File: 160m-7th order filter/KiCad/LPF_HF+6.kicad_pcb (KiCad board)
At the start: 2 copper layers, 250 x 160 mm, 131 parts, among them J1 Conn_01x07, J2 12V INPUT, J3 LFP_IN, J4 Conn_01x07, J5 RF output, U1 AMS1117-5, U2 74AHC595, U3 ULN2003

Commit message: 160m Cheby7
Created and Updated 160m 7th Order Filter Design
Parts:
- added C52: 2005pF, LPF_Footprints:4x1206_2, B.Cu at (117.7, 100.1)
- added L22: T130-10, LPF_Footprints:T106-Inductor, F.Cu at (117.5, 109.9)
- C15: footprint Capacitor_SMD:C_1206_3216Metric -> Capacitor_SMD:C_1206_3216Metric_Pad1.33x1.80mm_HandSolder
- C26: value C_Small -> 2005pF; footprint LPF_Footprints:6x1206 -> LPF_Footprints:4x1206_2
- C31, C37: value 834p -> 1480p
- C32, C38: value C_Small -> 3560pF
- D16, D17, D18, D21, D22, D7, D8, D9: value SD12_SOD323 -> TVS SD12_SOD323
- D19, D20: value Schottky -> 1n4148 Schottky
- L12, L6: value L -> T130-10
- moved C32 38.6 mm to (117.4, 161.8), turned to 180 degrees
- moved C38 24.6 mm to (117.4, 133.8)
- moved L12 22.9 mm to (117.5, 137.2)
- moved L6 16.2 mm to (117.7, 164.5)
- moved C26 9.20 mm to (118.3, 177.4), turned to 45 degrees
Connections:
- REL12 pad 4: Net-(C38-Pad1) -> Net-(C52-Pad1)
- REL12 pad 7: Net-(C38-Pad1) -> Net-(C52-Pad1)
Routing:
- net Net-(C52-Pad1): track 0.00 -> 35.4 mm
- net Net-(C38-Pad1): track 39.7 -> 14.6 mm
- net Net-(C26-Pad1): track 43.6 -> 27.4 mm
- net Net-(C32-Pad1): track 21.3 -> 14.7 mm
- net GND: vias 1017 -> 1020

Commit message: General Save
Minor updates and improvements
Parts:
- C32, C38: footprint LPF_Footprints:6x1206 -> LPF_Footprints:6x1206_3x2
- L1, L13, L7: value L -> Air core; footprint LPF_Footprints:T94-Inductor -> LPF_Footprints:T106-Inductor
- L10, L11, L14, L15, L16, L17, L2, L3, L4, L5, L8, L9: value L -> T106-10; footprint LPF_Footprints:T94-Inductor -> LPF_Footprints:T106-Inductor
- moved C32 0.69 mm to (117.4, 161.1)
- moved L19 0.24 mm to (312.8, 149.4)

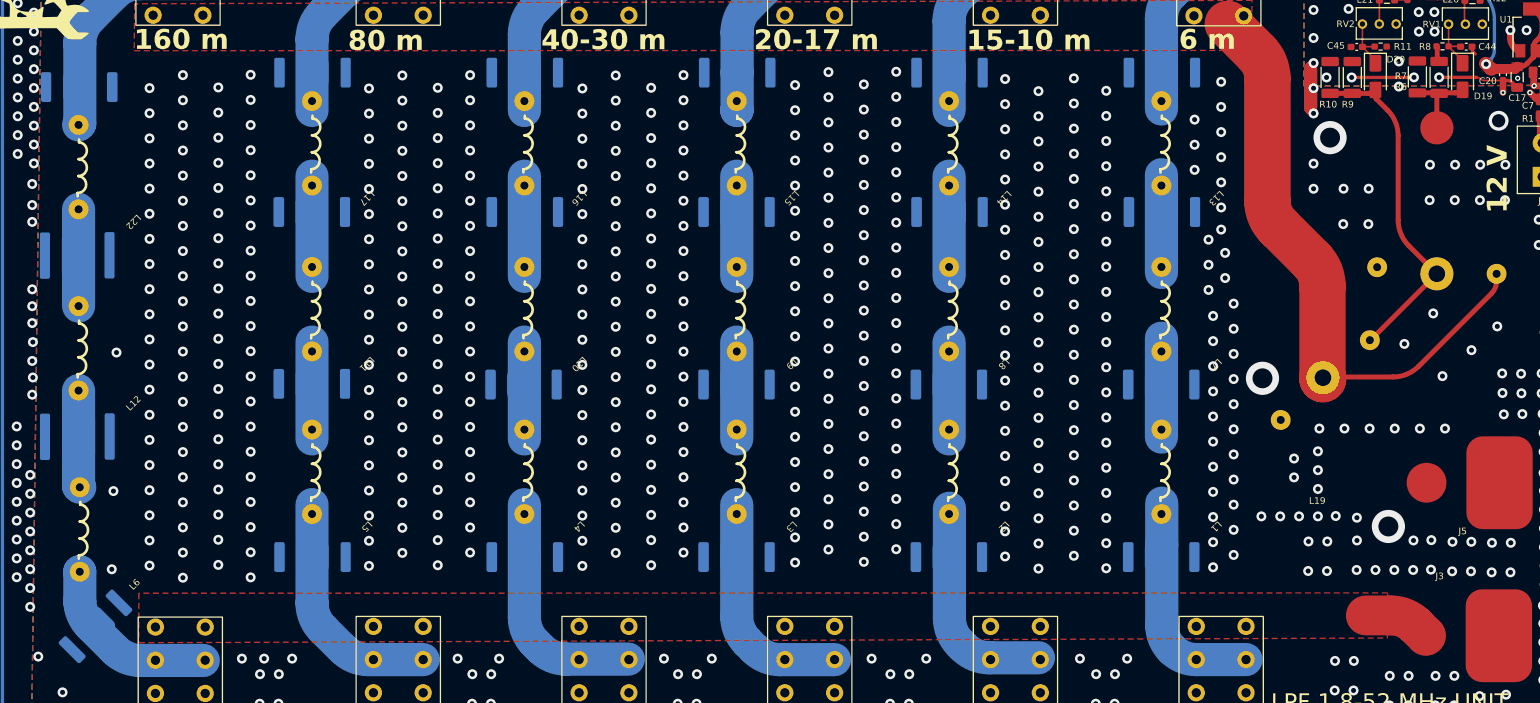
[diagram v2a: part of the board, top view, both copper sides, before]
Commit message: LPF capacitor and toroid selections improved
Added separate sheet for documenting capacitor makeup.
reflected in BOM much more accurately.
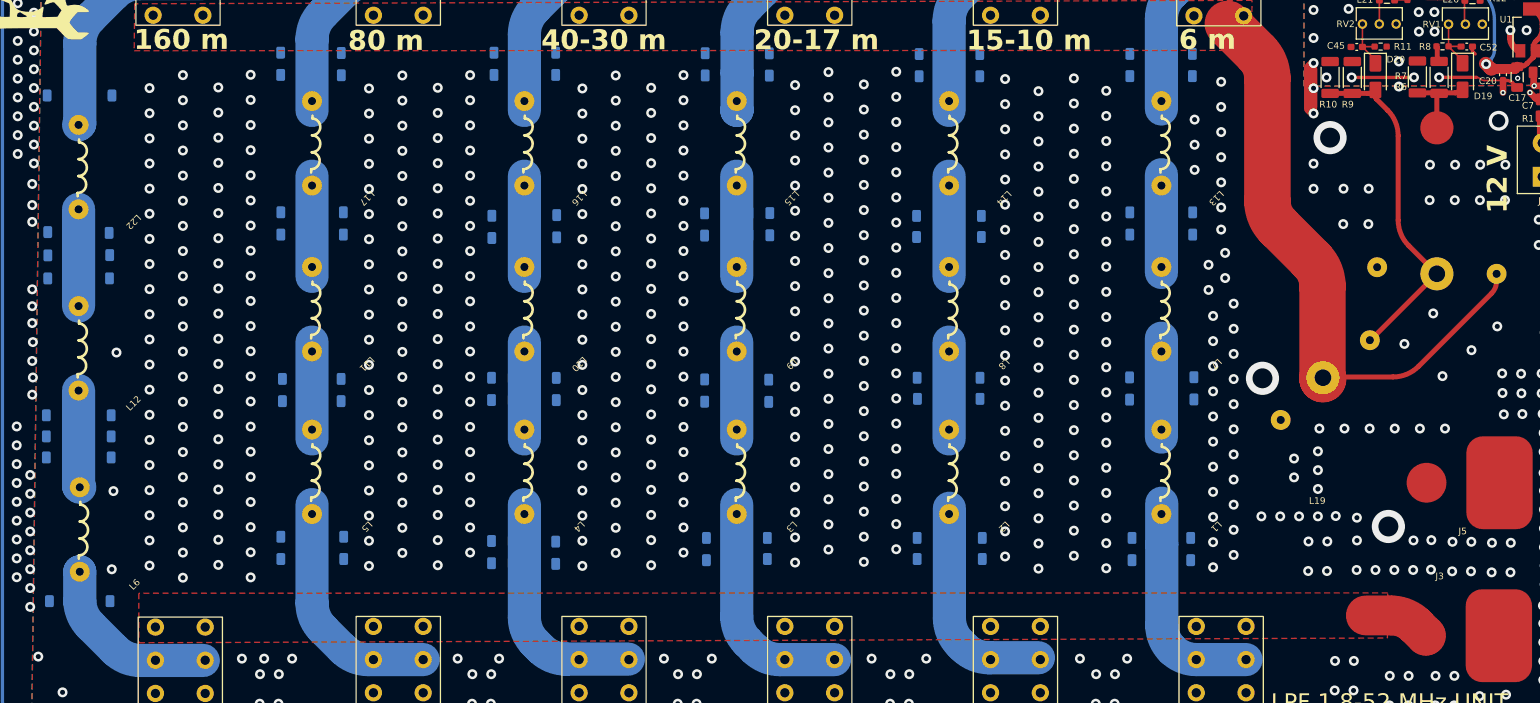
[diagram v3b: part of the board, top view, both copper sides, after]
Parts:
- removed C21, C39: 71p, LPF_Footprints:4x1206_2
- removed C22, C40: 123p, LPF_Footprints:4x1206_2
- removed C23, C41: 203p, LPF_Footprints:4x1206_2
- removed C24, C42: 357p, LPF_Footprints:4x1206_2
- removed C25, C43: 834p, LPF_Footprints:4x1206_2
- removed C26: 2005pF, LPF_Footprints:4x1206_2
- removed C27, C33: 127p, LPF_Footprints:4x1206_2
- removed C28, C34: 218p, LPF_Footprints:4x1206_2
- removed C29, C35: 360p, LPF_Footprints:4x1206_2
- removed C30, C36: 635p, LPF_Footprints:4x1206_2
- removed C31, C37: 1480p, LPF_Footprints:4x1206_2
- removed C32, C38: 3560pF, LPF_Footprints:6x1206_3x2
- removed C44: 100n, Capacitor_SMD:C_0603_1608Metric_Pad1.08x0.95mm_HandSolder
- added C21.1: 33p, Capacitor_SMD:C_1206_3216Metric_Pad1.33x1.80mm_HandSolder, B.Cu at (277.8, 165.7)
- added C21.2: 22p, Capacitor_SMD:C_1206_3216Metric_Pad1.33x1.80mm_HandSolder, B.Cu at (277.8, 169.1)
- added C21.3: 10p, Capacitor_SMD:C_1206_3216Metric_Pad1.33x1.80mm_HandSolder, B.Cu at (283.5, 169.1)
- added C21.4: 10p, Capacitor_SMD:C_1206_3216Metric_Pad1.33x1.80mm_HandSolder, B.Cu at (283.5, 165.7)
- added C22.1: 47p, Capacitor_SMD:C_1206_3216Metric_Pad1.33x1.80mm_HandSolder, B.Cu at (245.4, 165.7)
- added C22.2: 33p, Capacitor_SMD:C_1206_3216Metric_Pad1.33x1.80mm_HandSolder, B.Cu at (245.4, 168.9)
- added C22.3: 33p, Capacitor_SMD:C_1206_3216Metric_Pad1.33x1.80mm_HandSolder, B.Cu at (252.1, 165.7)
- added C22.4: 10p, Capacitor_SMD:C_1206_3216Metric_Pad1.33x1.80mm_HandSolder, B.Cu at (252.1, 168.9)
- added C23.1: 51p, Capacitor_SMD:C_1206_3216Metric_Pad1.33x1.80mm_HandSolder, B.Cu at (213.7, 165.7)
- added C23.2: 51p, Capacitor_SMD:C_1206_3216Metric_Pad1.33x1.80mm_HandSolder, B.Cu at (213.7, 169.1)
- added C23.3: 51p, Capacitor_SMD:C_1206_3216Metric_Pad1.33x1.80mm_HandSolder, B.Cu at (219.7, 165.7)
- added C23.4: 51p, Capacitor_SMD:C_1206_3216Metric_Pad1.33x1.80mm_HandSolder, B.Cu at (219.7, 168.9)
- added C24.1: 100p, Capacitor_SMD:C_1206_3216Metric_Pad1.33x1.80mm_HandSolder, B.Cu at (181.3, 166.2)
- added C24.2: 100p, Capacitor_SMD:C_1206_3216Metric_Pad1.33x1.80mm_HandSolder, B.Cu at (181.3, 169.5)
- added C24.3: 100p, Capacitor_SMD:C_1206_3216Metric_Pad1.33x1.80mm_HandSolder, B.Cu at (187.8, 169.6)
- added C24.4: 51p, Capacitor_SMD:C_1206_3216Metric_Pad1.33x1.80mm_HandSolder, B.Cu at (187.8, 166.3)
- added C25.1: 220p, Capacitor_SMD:C_1206_3216Metric_Pad1.33x1.80mm_HandSolder, B.Cu at (149.5, 165.6)
- added C25.2: 220p, Capacitor_SMD:C_1206_3216Metric_Pad1.33x1.80mm_HandSolder, B.Cu at (149.5, 168.9)
- added C25.3: 220p, Capacitor_SMD:C_1206_3216Metric_Pad1.33x1.80mm_HandSolder, B.Cu at (155.9, 168.9)
- added C25.4: 180p, Capacitor_SMD:C_1206_3216Metric_Pad1.33x1.80mm_HandSolder, B.Cu at (155.9, 165.6)
- added C26.1: 1000p, Capacitor_SMD:C_1206_3216Metric_Pad1.33x1.80mm_HandSolder, B.Cu at (120.7, 175.3)
- added C26.2: 1000p, Capacitor_SMD:C_1206_3216Metric_Pad1.33x1.80mm_HandSolder, B.Cu at (114.6, 175.3)
- added C27.1: 33p, Capacitor_SMD:C_1206_3216Metric_Pad1.33x1.80mm_HandSolder, B.Cu at (277.4, 141.5)
- added C27.2: 33p, Capacitor_SMD:C_1206_3216Metric_Pad1.33x1.80mm_HandSolder, B.Cu at (277.4, 144.9)
- added C27.3: 33p, Capacitor_SMD:C_1206_3216Metric_Pad1.33x1.80mm_HandSolder, B.Cu at (284.0, 144.9)
- added C27.4: 22p, Capacitor_SMD:C_1206_3216Metric_Pad1.33x1.80mm_HandSolder, B.Cu at (284.0, 141.5)
- added C28.1: 100p, Capacitor_SMD:C_1206_3216Metric_Pad1.33x1.80mm_HandSolder, B.Cu at (251.8, 141.6)
- added C28.2: 47p, Capacitor_SMD:C_1206_3216Metric_Pad1.33x1.80mm_HandSolder, B.Cu at (251.8, 144.8)
- added C28.3: 47p, Capacitor_SMD:C_1206_3216Metric_Pad1.33x1.80mm_HandSolder, B.Cu at (245.5, 144.8)
- added C28.4: 22p, Capacitor_SMD:C_1206_3216Metric_Pad1.33x1.80mm_HandSolder, B.Cu at (245.4, 141.6)
- added C29.1: 220p, Capacitor_SMD:C_1206_3216Metric_Pad1.33x1.80mm_HandSolder, B.Cu at (213.4, 141.9)
- added C29.2: 47p, Capacitor_SMD:C_1206_3216Metric_Pad1.33x1.80mm_HandSolder, B.Cu at (213.4, 145.2)
- added C29.3: 47p, Capacitor_SMD:C_1206_3216Metric_Pad1.33x1.80mm_HandSolder, B.Cu at (219.9, 145.2)
- added C29.4: 47p, Capacitor_SMD:C_1206_3216Metric_Pad1.33x1.80mm_HandSolder, B.Cu at (219.9, 141.9)
- added C30.1: 180p, Capacitor_SMD:C_1206_3216Metric_Pad1.33x1.80mm_HandSolder, B.Cu at (181.3, 141.6)
- added C30.2: 180p, Capacitor_SMD:C_1206_3216Metric_Pad1.33x1.80mm_HandSolder, B.Cu at (181.3, 145.0)
- added C30.3: 180p, Capacitor_SMD:C_1206_3216Metric_Pad1.33x1.80mm_HandSolder, B.Cu at (187.9, 145.0)
- added C30.4: 100p, Capacitor_SMD:C_1206_3216Metric_Pad1.33x1.80mm_HandSolder, B.Cu at (187.9, 141.6)
- added C31.1: 470p, Capacitor_SMD:C_1206_3216Metric_Pad1.33x1.80mm_HandSolder, B.Cu at (155.5, 141.8)
- added C31.2: 470p, Capacitor_SMD:C_1206_3216Metric_Pad1.33x1.80mm_HandSolder, B.Cu at (155.5, 145.1)
- added C31.3: 470p, Capacitor_SMD:C_1206_3216Metric_Pad1.33x1.80mm_HandSolder, B.Cu at (149.8, 141.8)
- added C31.4: 51p, Capacitor_SMD:C_1206_3216Metric_Pad1.33x1.80mm_HandSolder, B.Cu at (149.8, 145.1)
- added C32.1: 1000p, Capacitor_SMD:C_1206_3216Metric_Pad1.33x1.80mm_HandSolder, B.Cu at (120.8, 147.3)
- added C32.2: 1000p, Capacitor_SMD:C_1206_3216Metric_Pad1.33x1.80mm_HandSolder, B.Cu at (120.8, 150.4)
- added C32.3: 1000p, Capacitor_SMD:C_1206_3216Metric_Pad1.33x1.80mm_HandSolder, B.Cu at (120.8, 153.6)
- added C32.4: 470p, Capacitor_SMD:C_1206_3216Metric_Pad1.33x1.80mm_HandSolder, B.Cu at (114.2, 147.3)
- added C32.5: 47p, Capacitor_SMD:C_1206_3216Metric_Pad1.33x1.80mm_HandSolder, B.Cu at (114.2, 150.4)
- added C32.6: 47p, Capacitor_SMD:C_1206_3216Metric_Pad1.33x1.80mm_HandSolder, B.Cu at (114.2, 153.6)
- added C33.1: 33p, Capacitor_SMD:C_1206_3216Metric_Pad1.33x1.80mm_HandSolder, B.Cu at (277.5, 116.7)
- added C33.2: 33p, Capacitor_SMD:C_1206_3216Metric_Pad1.33x1.80mm_HandSolder, B.Cu at (277.5, 120.0)
- added C33.3: 33p, Capacitor_SMD:C_1206_3216Metric_Pad1.33x1.80mm_HandSolder, B.Cu at (283.8, 120.0)
- added C33.4: 22p, Capacitor_SMD:C_1206_3216Metric_Pad1.33x1.80mm_HandSolder, B.Cu at (283.8, 116.7)
- added C34.1: 100p, Capacitor_SMD:C_1206_3216Metric_Pad1.33x1.80mm_HandSolder, B.Cu at (245.3, 117.2)
- added C34.2: 47p, Capacitor_SMD:C_1206_3216Metric_Pad1.33x1.80mm_HandSolder, B.Cu at (245.3, 120.4)
- added C34.3: 47p, Capacitor_SMD:C_1206_3216Metric_Pad1.33x1.80mm_HandSolder, B.Cu at (252.0, 117.2)
- added C34.4: 22p, Capacitor_SMD:C_1206_3216Metric_Pad1.33x1.80mm_HandSolder, B.Cu at (252.0, 120.4)
- added C35.1: 220p, Capacitor_SMD:C_1206_3216Metric_Pad1.33x1.80mm_HandSolder, B.Cu at (220.1, 116.8)
- added C35.2: 47p, Capacitor_SMD:C_1206_3216Metric_Pad1.33x1.80mm_HandSolder, B.Cu at (220.1, 120.1)
- added C35.3: 47p, Capacitor_SMD:C_1206_3216Metric_Pad1.33x1.80mm_HandSolder, B.Cu at (213.4, 116.8)
- added C35.4: 47p, Capacitor_SMD:C_1206_3216Metric_Pad1.33x1.80mm_HandSolder, B.Cu at (213.4, 120.2)
- added C36.1: 180p, Capacitor_SMD:C_1206_3216Metric_Pad1.33x1.80mm_HandSolder, B.Cu at (188.0, 120.4)
- added C36.2: 180p, Capacitor_SMD:C_1206_3216Metric_Pad1.33x1.80mm_HandSolder, B.Cu at (188.0, 117.1)
- added C36.3: 180p, Capacitor_SMD:C_1206_3216Metric_Pad1.33x1.80mm_HandSolder, B.Cu at (181.3, 117.2)
- added C36.4: 100p, Capacitor_SMD:C_1206_3216Metric_Pad1.33x1.80mm_HandSolder, B.Cu at (181.3, 120.5)
- added C37.1: 470p, Capacitor_SMD:C_1206_3216Metric_Pad1.33x1.80mm_HandSolder, B.Cu at (149.5, 116.7)
- added C37.2: 470p, Capacitor_SMD:C_1206_3216Metric_Pad1.33x1.80mm_HandSolder, B.Cu at (149.5, 120.0)
- added C37.3: 470p, Capacitor_SMD:C_1206_3216Metric_Pad1.33x1.80mm_HandSolder, B.Cu at (155.8, 120.0)
- added C37.4: 51p, Capacitor_SMD:C_1206_3216Metric_Pad1.33x1.80mm_HandSolder, B.Cu at (155.8, 116.7)
- added C38.1: 1000p, Capacitor_SMD:C_1206_3216Metric_Pad1.33x1.80mm_HandSolder, B.Cu at (114.4, 119.6)
- added C38.2: 1000p, Capacitor_SMD:C_1206_3216Metric_Pad1.33x1.80mm_HandSolder, B.Cu at (114.4, 123.2)
- added C38.3: 1000p, Capacitor_SMD:C_1206_3216Metric_Pad1.33x1.80mm_HandSolder, B.Cu at (114.4, 126.6)
- added C38.4: 470p, Capacitor_SMD:C_1206_3216Metric_Pad1.33x1.80mm_HandSolder, B.Cu at (120.5, 119.8)
- added C38.5: 47p, Capacitor_SMD:C_1206_3216Metric_Pad1.33x1.80mm_HandSolder, B.Cu at (120.6, 123.1)
- added C38.6: 47p, Capacitor_SMD:C_1206_3216Metric_Pad1.33x1.80mm_HandSolder, B.Cu at (120.6, 126.6)
- added C39.1: 33p, Capacitor_SMD:C_1206_3216Metric_Pad1.33x1.80mm_HandSolder, B.Cu at (277.5, 92.8)
- added C39.2: 22p, Capacitor_SMD:C_1206_3216Metric_Pad1.33x1.80mm_HandSolder, B.Cu at (277.5, 96.1)
- added C39.3: 10p, Capacitor_SMD:C_1206_3216Metric_Pad1.33x1.80mm_HandSolder, B.Cu at (283.8, 96.1)
- added C39.4: 10p, Capacitor_SMD:C_1206_3216Metric_Pad1.33x1.80mm_HandSolder, B.Cu at (283.8, 92.8)
- added C40.1: 47p, Capacitor_SMD:C_1206_3216Metric_Pad1.33x1.80mm_HandSolder, B.Cu at (245.7, 92.8)
- added C40.2: 33p, Capacitor_SMD:C_1206_3216Metric_Pad1.33x1.80mm_HandSolder, B.Cu at (245.7, 96.2)
- added C40.3: 33p, Capacitor_SMD:C_1206_3216Metric_Pad1.33x1.80mm_HandSolder, B.Cu at (251.7, 96.2)
- added C40.4: 10p, Capacitor_SMD:C_1206_3216Metric_Pad1.33x1.80mm_HandSolder, B.Cu at (251.7, 92.8)
- added C41.1: 51p, Capacitor_SMD:C_1206_3216Metric_Pad1.33x1.80mm_HandSolder, B.Cu at (213.5, 92.7)
- added C41.2: 51p, Capacitor_SMD:C_1206_3216Metric_Pad1.33x1.80mm_HandSolder, B.Cu at (213.5, 96.0)
- added C41.3: 51p, Capacitor_SMD:C_1206_3216Metric_Pad1.33x1.80mm_HandSolder, B.Cu at (220.0, 96.1)
- added C41.4: 51p, Capacitor_SMD:C_1206_3216Metric_Pad1.33x1.80mm_HandSolder, B.Cu at (220.0, 92.7)
- added C42.1: 100p, Capacitor_SMD:C_1206_3216Metric_Pad1.33x1.80mm_HandSolder, B.Cu at (181.6, 92.6)
- added C42.2: 100p, Capacitor_SMD:C_1206_3216Metric_Pad1.33x1.80mm_HandSolder, B.Cu at (181.6, 96.0)
- added C42.3: 100p, Capacitor_SMD:C_1206_3216Metric_Pad1.33x1.80mm_HandSolder, B.Cu at (187.8, 96.0)
- added C42.4: 51p, Capacitor_SMD:C_1206_3216Metric_Pad1.33x1.80mm_HandSolder, B.Cu at (187.8, 92.6)
- added C43.1: 220p, Capacitor_SMD:C_1206_3216Metric_Pad1.33x1.80mm_HandSolder, B.Cu at (149.5, 92.6)
- added C43.2: 220p, Capacitor_SMD:C_1206_3216Metric_Pad1.33x1.80mm_HandSolder, B.Cu at (149.5, 96.0)
- added C43.3: 220p, Capacitor_SMD:C_1206_3216Metric_Pad1.33x1.80mm_HandSolder, B.Cu at (155.5, 96.0)
- added C43.4: 180p, Capacitor_SMD:C_1206_3216Metric_Pad1.33x1.80mm_HandSolder, B.Cu at (155.5, 92.7)
- added C44.1: 1000p, Capacitor_SMD:C_1206_3216Metric_Pad1.33x1.80mm_HandSolder, B.Cu at (114.3, 99.1)
- added C44.2: 1000p, Capacitor_SMD:C_1206_3216Metric_Pad1.33x1.80mm_HandSolder, B.Cu at (120.9, 99.1)
- C52: value 2005pF -> 100n; footprint LPF_Footprints:4x1206_2 -> Capacitor_SMD:C_0603_1608Metric_Pad1.08x0.95mm_HandSolder; moved to F.Cu
- moved C52 209.2 mm to (326.7, 91.7), turned to 0 degrees
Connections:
- net /20-17m renamed /20-17m_REL
- net Net-(C21-Pad1) renamed C21
- net Net-(C22-Pad1) renamed C22
- net Net-(C23-Pad1) renamed C23
- net Net-(C24-Pad1) renamed C24
- net Net-(C25-Pad1) renamed C25
- net Net-(C26-Pad1) renamed C26
- net Net-(C27-Pad1) renamed C27
- net Net-(C28-Pad1) renamed C28
- net Net-(C29-Pad1) renamed C29
- net Net-(C30-Pad1) renamed C30
- net Net-(C31-Pad1) renamed C31
- net Net-(C32-Pad1) renamed C32
- net Net-(C33-Pad1) renamed C33
- net Net-(C34-Pad1) renamed C34
- net Net-(C35-Pad1) renamed C35
- net Net-(C36-Pad1) renamed C36
- net Net-(C37-Pad1) renamed C37
- net Net-(C38-Pad1) renamed C38
- net Net-(C39-Pad1) renamed C39
- net Net-(C40-Pad1) renamed C40
- net Net-(C41-Pad1) renamed C41
- net Net-(C42-Pad1) renamed C42
- net Net-(C43-Pad1) renamed C43
- C52 pad 1: Net-(C52-Pad1) -> Net-(D19-K)
- L22 pad 2: Net-(C52-Pad1) -> C44
- REL12 pad 4: Net-(C52-Pad1) -> C44
- REL12 pad 7: Net-(C52-Pad1) -> C44
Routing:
- net Net-(C52-Pad1): track 35.4 -> 0.00 mm
- net C44: track 0.00 -> 35.4 mm
- net GND: vias 1020 -> 1019
